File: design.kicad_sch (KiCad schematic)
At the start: 51 parts, among them SW1 EN, SW2 IO0, U1 TCK127BG, U2 AP3015, U3 ESP32-C3-WROOM-02-N4, U4 TTP223

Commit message: Update design.kicad_sch
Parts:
- removed JP2, JP?: AHLB, Jumper:SolderJumper-2_P1.3mm_Bridged_RoundedPad1.0x1.5mm, symbol Jumper:Jumper_2_Bridged
- added C1: C_Small, Capacitor_SMD:C_0805_2012Metric, symbol Device:C_Small
- added D1: SS14, Diode_SMD:D_SMA, symbol Device:D_Schottky_Small
- added JP1: Switch_jump, Jumper:SolderJumper-2_P1.3mm_Open_RoundedPad1.0x1.5mm, symbol Jumper:Jumper_2_Open
- added JP2: Reg_jump, Jumper:SolderJumper-2_P1.3mm_Open_RoundedPad1.0x1.5mm, symbol Jumper:Jumper_2_Open
- added JP3: SHDN-Control, Jumper:SolderJumper-3_P1.3mm_Bridged12_RoundedPad1.0x1.5mm_NumberLabels, symbol Jumper:SolderJumper_3_Bridged12
- added JP6, JP7: AHLB, Jumper:SolderJumper-2_P1.3mm_Open_RoundedPad1.0x1.5mm, symbol Jumper:Jumper_2_Open
- added R11, R12: 10K, Resistor_SMD:R_0805_2012Metric, symbol Device:R_Small
- C2: value C_Small -> 4.7uF
- C3: renamed from C1; value C_Small -> 10pF
- C4: renamed from C3; value C_Small -> 20uF
- D2, D6, D7: renamed from D?; footprint (none) -> Diode_SMD:D_SOD-323
- D3, D4, D5: renamed from D?; footprint (none) -> LED_SMD:LED_0603_1608Metric
- H1, H2, H3, H4: renamed from H?; footprint (none) -> MountingHole:MountingHole_3.2mm_M3
- J1: renamed from J?; footprint (none) -> Connector_PinSocket_2.54mm:PinSocket_2x06_P2.54mm_Vertical_SMD
- J2: renamed from J?; footprint (none) -> Connector_PinHeader_2.54mm:PinHeader_1x04_P2.54mm_Vertical
- L1: value L_Small -> 10uH
- R1: value R_Small -> 1M
- R2: value R_Small -> 600k
- SW1: renamed from SW?; footprint (none) -> Button_Switch_SMD:SW_SPST_EVPBF
- TP1, TP2, TP3: renamed from TP?; footprint (none) -> TestPoint:TestPoint_Pad_D2.5mm
- gave numbers to parts that had none: 13
- renumbered C8 to C10, C4 to C5, C5 to C6, C6 to C7, C7 to C8, JP1 to JP4, R3 to R6, R4 to R7, SW1 to SW2, SW2 to SW3
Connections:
- net IO18 is gone; now on net D-: J1.11 (Pin_11), U3.13 (IO18)
- net IO19 is gone; now on net D+: J1.12 (Pin_12), U3.14 (IO19)
- net +3.3V: now also D1.1 (K), JP2.2 (B), R11.1, R12.1; no longer L1.2, U2.1 (SW)
- net GND: now also R3.1, R4.1, C1.2; no longer R3.2, R4.2
- net IO2: now also R11.2
- net IO6: now also JP3.3 (B)
- net IO8: now also R12.2
- net VCC: now also C1.1, JP1.1 (A), JP6.2 (B), JP7.2 (B)
- net at C2.1, L1.1, U1.A1 (VOUT)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: now also JP1.2 (B), JP2.1 (A), JP3.1 (A); no longer U2.4 (~{SHDN})
- net at J3.A5 (CC1): now also R4.2; no longer R3.1
- net at U5.4 (AHLB): now also JP7.1 (A)
- net at U4.4 (AHLB): now also JP6.1 (A)
- net D+: now reaches J3.A6 (D+)
- net D+: now also J3.B6 (D+)
- net D-: now reaches J3.A7 (D-)
- net D-: now also J3.B7 (D-)
- net at J3.B5 (CC2): now also R3.2; no longer R4.1
- new net: D1.2 (A), L1.2, U2.1 (SW)
- new net: JP3.2 (C), U2.4 (~{SHDN})
- no-connect marks 14 -> 10
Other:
- note added: "Input"
- note added: "MCU"
- note added: "Pads + Mechanical"
- note added: "SUMIDA CDRH4D16FB/NP-100MC"
- note added: "Status"
- note added: "TOG: LOW - Direct Mode HIGH - Toggle Mode AHLB: LOW - CMOS active high output HIGH - CMOS active low output"
- note added: "Touch"
- note added: "VOUT = 1.23V*(1+R1/R2) 3.3V = 1.23V*(1+1MOhm/600kOhm)"
- note added: "Vbat = VCC: 0.9-1.5 - single cell 1.8-3.0 - dual cell"
- note added: "enable > 0.9V disable < 0.25V"
- note added: "enable > 0.9V disable < 0.4V"
- moved on the sheet: C10, C11, C2, C3, C4, C5, C6, C7, C8, C9, D2, D3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

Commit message: PCB scramble
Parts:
- J3: footprint Connector_USB:USB_C_Receptacle_HRO_TYPE-C-31-M-12_simple -> Connector_USB:USB_C_Receptacle_HRO_TYPE-C-31-M-12
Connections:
- net D+: no longer J1.12 (Pin_12)
- net D-: no longer J1.11 (Pin_11)
- net IO0: now reaches R7.2, SW3.2, U3.18 (IO0)
- net SW: now reaches D1.2 (A), L1.2, U2.1 (SW)
- net FB: now reaches R1.2, R2.1, U2.3 (FB)
- net SHDN: now reaches JP3.2 (C), U2.4 (~{SHDN})
- net In: now reaches C2.1, JP1.2 (B), JP2.1 (A), JP3.1 (A), L1.1, U1.A1 (VOUT), U2.5 (IN)
- net CC2: now reaches J3.B5 (CC2), R3.2
- net EN: now reaches C7.1, R6.2, SW2.2, U3.2 (EN)
- net CC1: now reaches J3.A5 (CC1), R4.2
- net control: now reaches D2.2 (A), SW1.1
- no-connect marks 10 -> 12

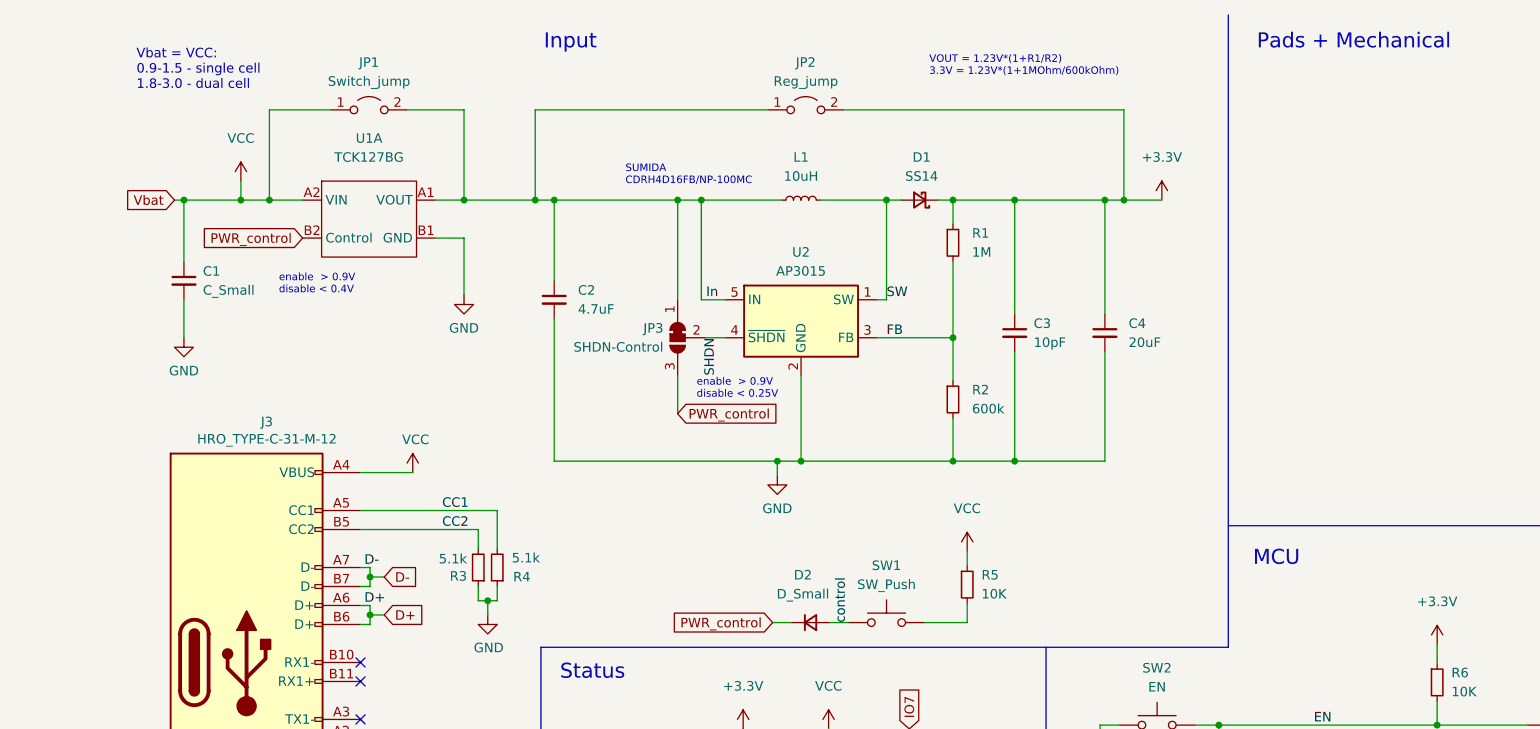
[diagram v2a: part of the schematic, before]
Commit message: cleaning up
silkscreen
info text
description
adding warning about unfinished input voltage rail
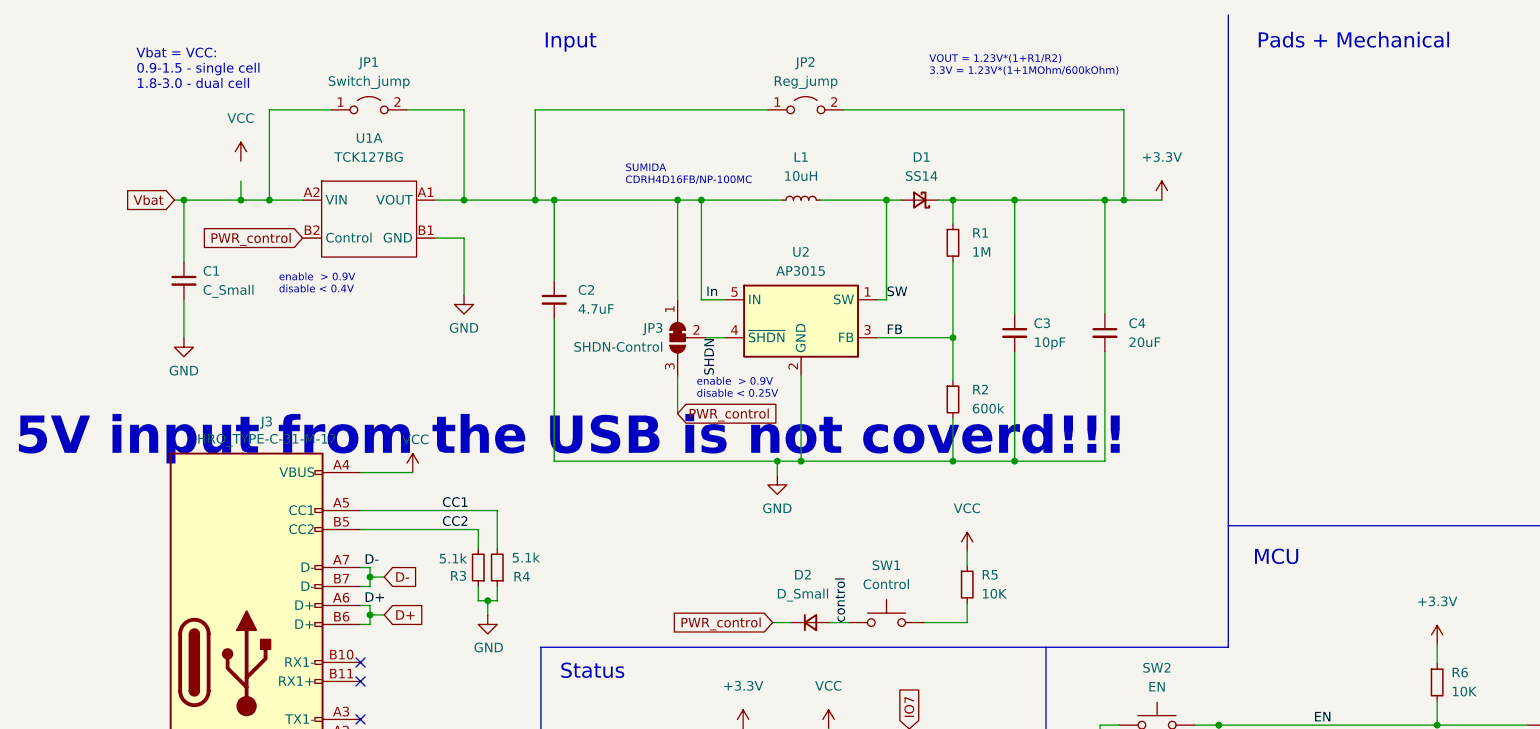
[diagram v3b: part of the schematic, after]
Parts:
- SW1: value SW_Push -> Control
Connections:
- net VCC: no longer C1.1, JP1.1 (A), U1.A2 (VIN)
- new net Vbat: C1.1, JP1.1 (A), U1.A2 (VIN)
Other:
- note added: "5V input from the USB is not coverd!!!"
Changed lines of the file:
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@@
     (effects (font (size 2 2)) (justify left bottom))
+  )
+  (text "5V input from the USB is not coverd!!!" (at -1.524 70.866 0)
+    (effects (font (size 5 5) (thickness 1) bold) (justify left bottom))
   )
   (text "enable  > 0.9V\ndisable < 0.4V" (at 33.782 48.895 0)
@@
     (pin "1")
   )
-  (symbol (lib_id "power:VCC") (at 28.702 33.655 0) (unit 1)
-    (in_bom yes) (on_board yes) (fields_autoplaced)
-    (property "Reference" "#PWR02" (id 0) (at 28.702 37.465 0)
-      (effects (font (size 1.27 1.27)) hide)
-    )
-    (property "Value" "VCC" (id 1) (at 28.702 27.94 0))
-    (property "Footprint" "" (id 2) (at 28.702 33.655 0)
-      (effects (font (size 1.27 1.27)) hide)
-    )
-    (property "Datasheet" "" (id 3) (at 28.702 33.655 0)
+  (symbol (lib_id "power:VCC") (at 28.702 30.988 0) (unit 1)
+    (in_bom yes) (on_board yes) (fields_autoplaced)
+    (property "Reference" "#PWR02" (id 0) (at 28.702 34.798 0)
+      (effects (font (size 1.27 1.27)) hide)
+    )
+    (property "Value" "VCC" (id 1) (at 28.702 25.273 0))
+    (property "Footprint" "" (id 2) (at 28.702 30.988 0)
+      (effects (font (size 1.27 1.27)) hide)
+    )
+    (property "Datasheet" "" (id 3) (at 28.702 30.988 0)
       (effects (font (size 1.27 1.27)) hide)
     )
@@
     (in_bom yes) (on_board yes) (fields_autoplaced)
     (property "Reference" "SW1" (id 0) (at 115.062 85.09 0))
-    (property "Value" "SW_Push" (id 1) (at 115.062 87.63 0))
+    (property "Value" "Control" (id 1) (at 115.062 87.63 0))
     (property "Footprint" "Button_Switch_SMD:SW_SPST_EVPBF" (id 2) (at 115.062 87.63 0)
       (effects (font (size 1.27 1.27)) hide)
@@
     )
     (path "/da4fa78e-18d8-4651-b351-fddc3d43c33b"
-      (reference "SW1") (unit 1) (value "SW_Push") (footprint "Button_Switch_SMD:SW_SPST_EVPBF")
+      (reference "SW1") (unit 1) (value "Control") (footprint "Button_Switch_SMD:SW_SPST_EVPBF")
     )
     (path "/b73a353f-162e-4cfe-91e4-88788163a5f0"

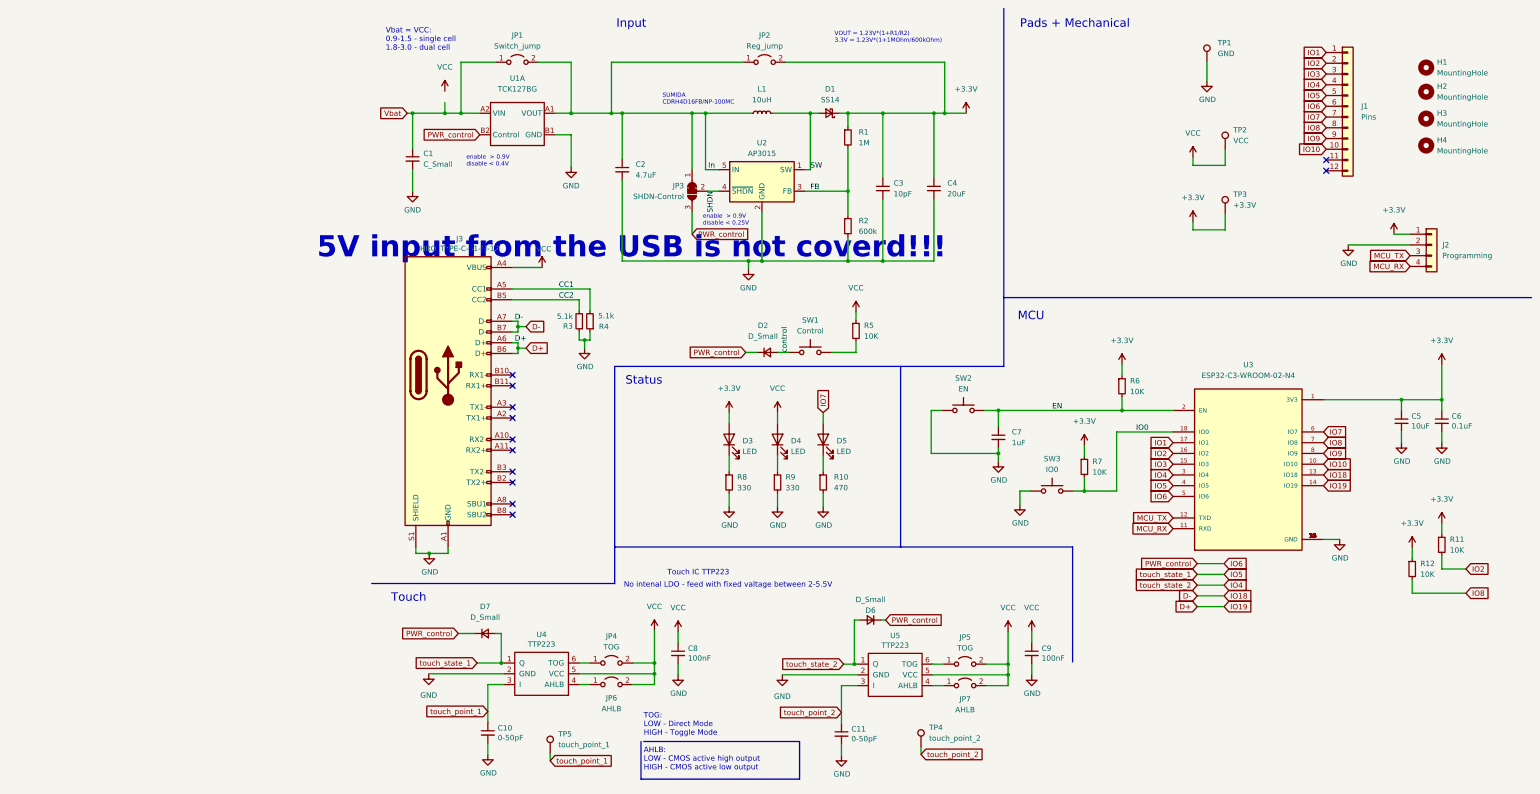
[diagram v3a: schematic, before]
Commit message: Add USB to 3.3V and powerpath USB/Vbat
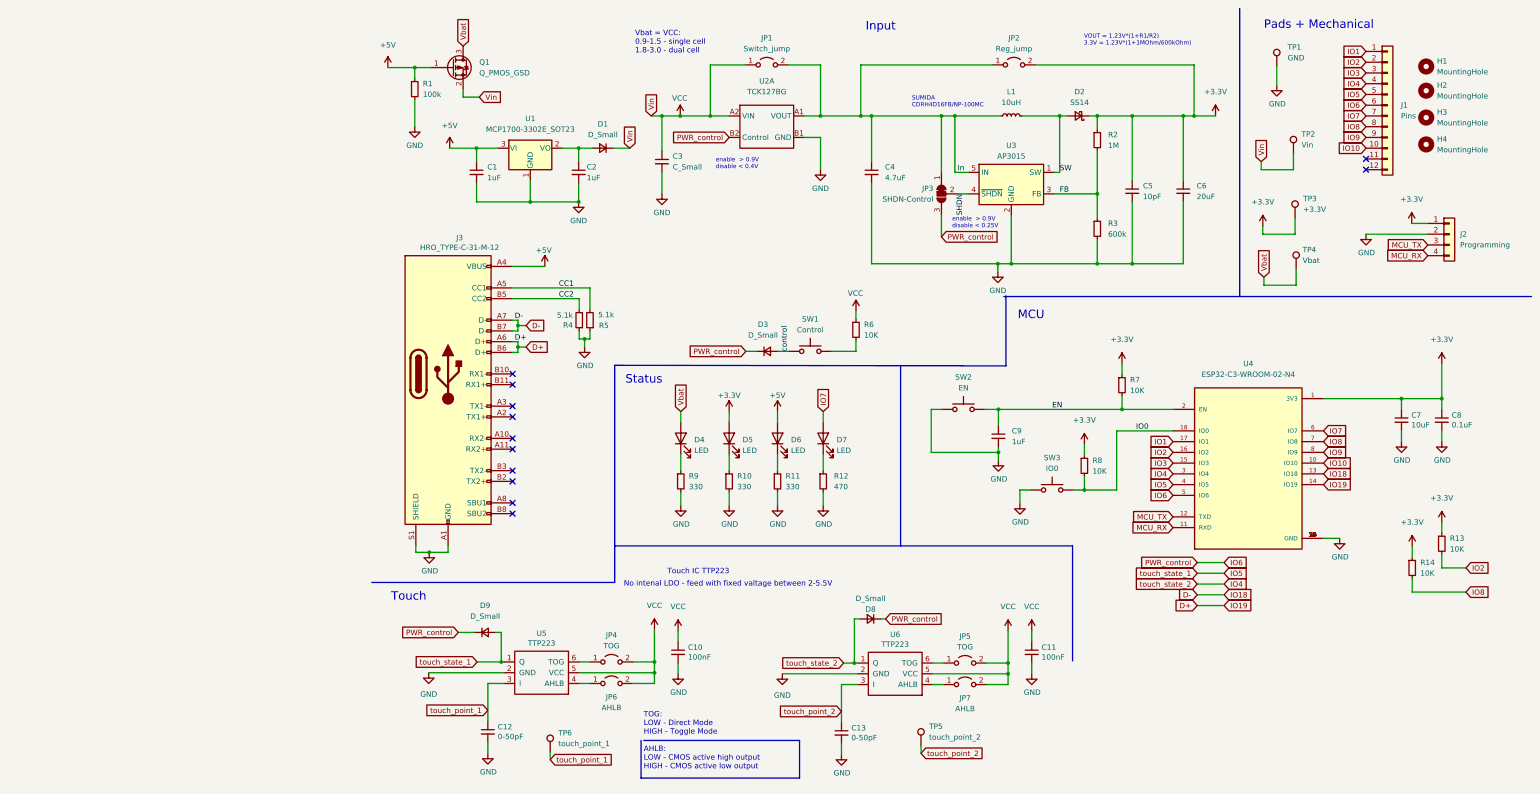
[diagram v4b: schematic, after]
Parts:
- added C1, C2: 1uF, Capacitor_SMD:C_0805_2012Metric, symbol Device:C_Small
- added D1: D_Small, Diode_SMD:D_SOD-323, symbol Device:D_Small
- added D4: LED, LED_SMD:LED_0603_1608Metric, symbol Device:LED
- added Q1: Q_PMOS_GSD, Package_TO_SOT_SMD:SOT-23, symbol Device:Q_PMOS_GSD
- added R1: 100k, Resistor_SMD:R_0805_2012Metric, symbol Device:R_Small
- added R9: 330, Resistor_SMD:R_0805_2012Metric, symbol Device:R_Small
- added TP4: Vbat, TestPoint:TestPoint_Pad_D2.5mm, symbol Connector:TestPoint
- added U1: MCP1700-3302E_SOT23, Package_TO_SOT_SMD:SOT-23, symbol Regulator_Linear:MCP1700-3302E_SOT23
- TP2: value VCC -> Vin
- renumbered C8 to C10, C9 to C11, C10 to C12, C11 to C13, C1 to C3, C2 to C4, C3 to C5, C4 to C6, C5 to C7, C6 to C8, C7 to C9, D1 to D2, D2 to D3, D3 to D5, D4 to D6, D5 to D7, D6 to D8, D7 to D9, R8 to R10, R9 to R11, R10 to R12, R11 to R13, R12 to R14, R1 to R2, R2 to R3, R3 to R4, R4 to R5, R5 to R6, R6 to R7, R7 to R8, TP4 to TP5, TP5 to TP6, U1 to U2, U2 to U3, U3 to U4, U4 to U5, U5 to U6
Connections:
- net GND: now also C1.2, C2.2, R1.2, R9.2, U1.1 (GND)
- net VCC: now also C3.1, JP1.1 (A), U2.A2 (VIN), D1.1 (K), Q1.2 (S); no longer D6.2 (A), J3.A4 (VBUS), J3.A9 (VBUS), J3.B4 (VBUS), J3.B9 (VBUS)
- net Vbat: now also D4.2 (A), Q1.3 (D), TP4.1; no longer C3.1, JP1.1 (A), U2.A2 (VIN)
- new net: D4.1 (K), R9.1
- new net: C2.1, D1.2 (A), U1.2 (VO)
- new net +5V: C1.1, D6.2 (A), J3.A4 (VBUS), J3.A9 (VBUS), J3.B4 (VBUS), J3.B9 (VBUS), Q1.1 (G), R1.1, U1.3 (VI)
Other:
- note removed: "5V input from the USB is not coverd!!!"
- moved on the sheet: C3, C4, C5, C6, D2, J1, J2, JP1, JP2, JP3, L1, R2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
